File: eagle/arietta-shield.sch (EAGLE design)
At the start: 11 parts

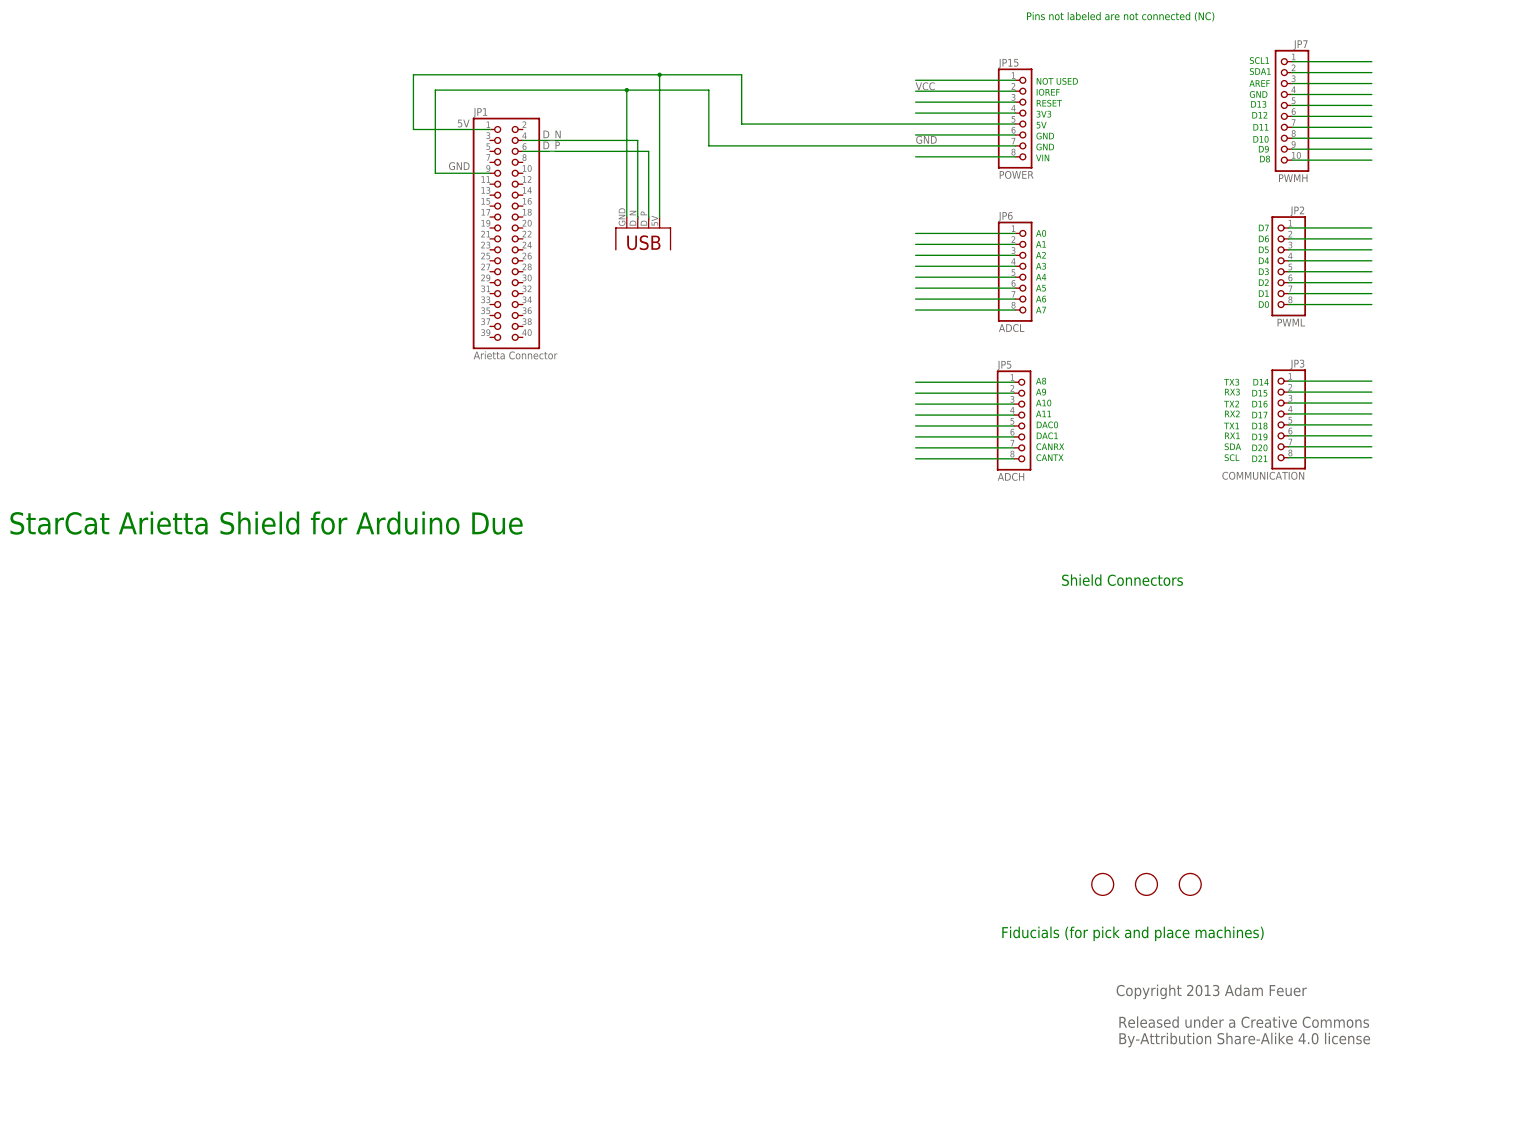
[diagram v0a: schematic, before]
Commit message: added unpopulated SPI and rear connectors
- 5V now only connected to USB now, not shield connector,
  enabling connection to another computer when connected to
  the Arduino Due
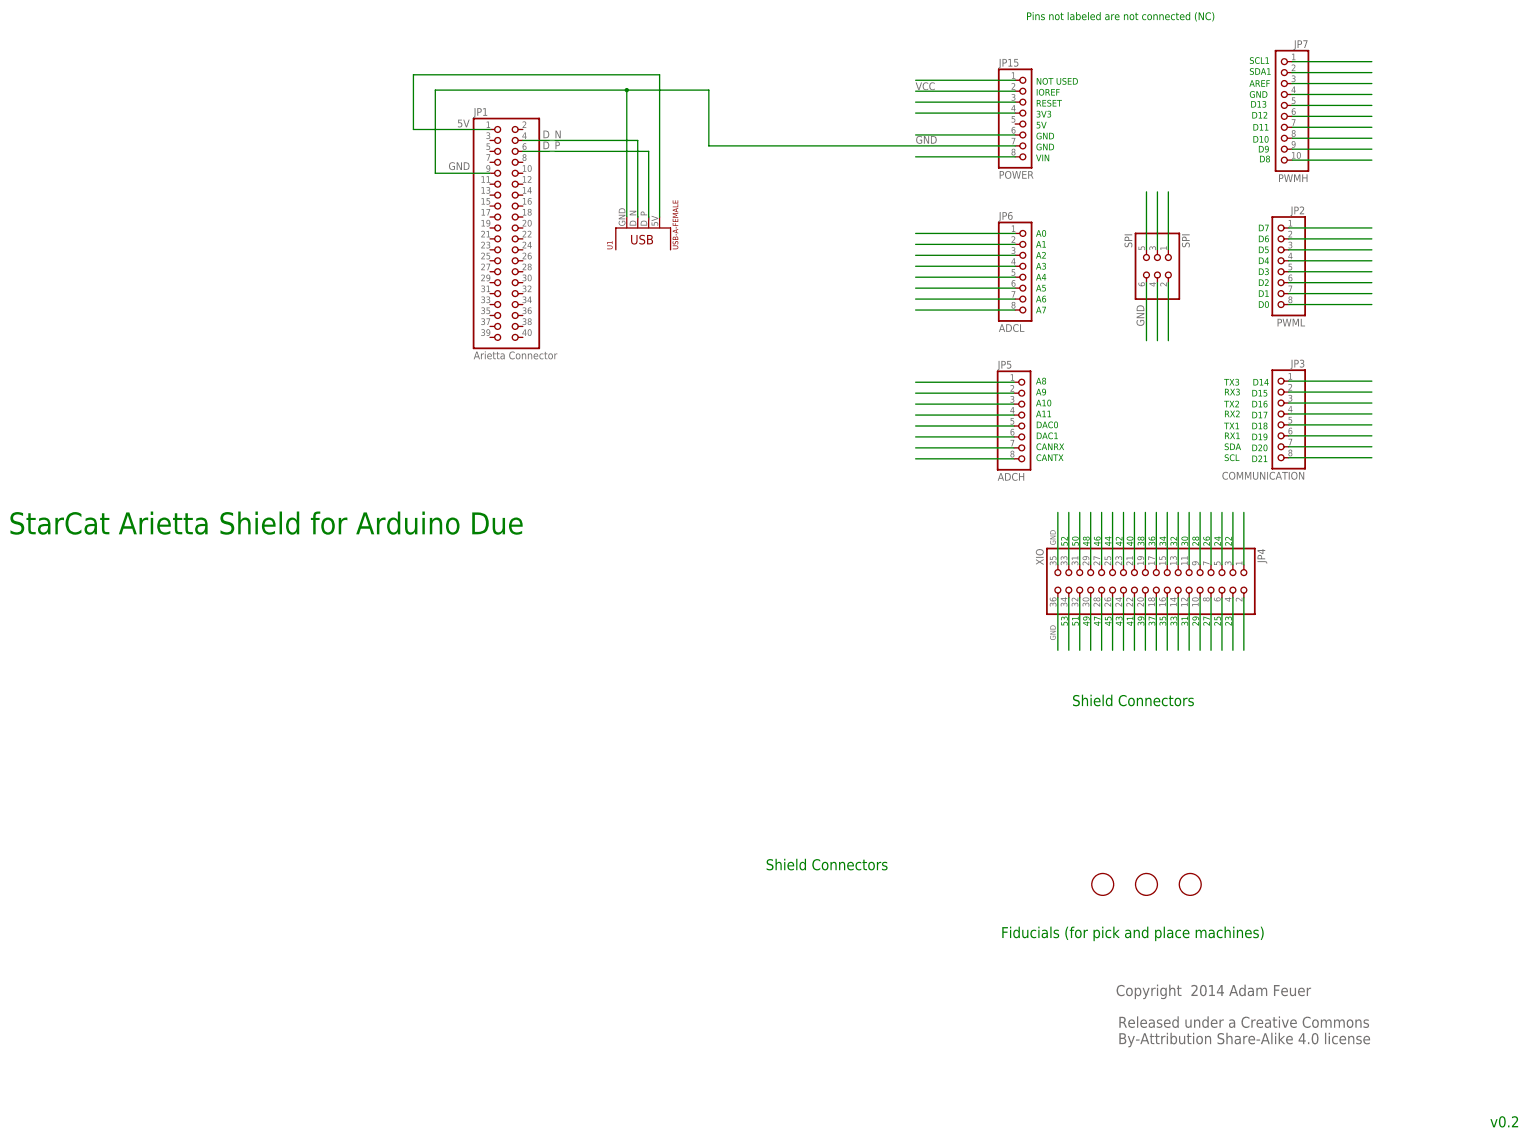
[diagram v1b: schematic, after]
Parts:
- added JP4: XIO, SmartPrj:PINHD-2X18
- added SPI: SPI, SmartPrj:PINHD-2X3
- renumbered U$7 to U1
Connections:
- new net D38: JP4.19
- new net D39: JP4.20
- new net D40: JP4.21
- new net D41: JP4.22
- new net D42: JP4.23
- new net D43: JP4.24
- new net D44: JP4.25
- new net D45: JP4.26
- new net N$109: JP4.31
- new net N$115: JP4.1
- new net N$116: JP4.2
- new net N$580: JP4.5
- new net N$581: JP4.7
- new net N$582: JP4.11
- new net N$583: JP4.13
- new net N$584: JP4.27
- new net N$585: JP4.29
- new net N$586: JP4.33
- new net N$587: JP4.4
- new net N$588: JP4.6
- new net N$589: JP4.8
- new net N$590: JP4.12
- new net N$591: JP4.14
- new net N$592: JP4.30
- new net N$601: JP4.28
- new net N$73: JP4.34
- new net N$74: JP4.32
- new net N$89: JP4.18
- new net N$91: JP4.16
- new net N$92: JP4.10
- new net N$93: JP4.3
- new net N$94: JP4.9
- new net N$96: JP4.15
- new net N$97: JP4.17
- new net RESET: SPI.5
- new net SPI0_MISO: SPI.1
- new net SPI0_MOSI: SPI.4
- new net SPI0_SCK: SPI.3
- new net VCC_5V: SPI.2
- net 5V: no longer JP15.5
- net GND: now also JP4.35, JP4.36, SPI.6
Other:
- note added: "22"
- note added: "23"
- note added: "24"
- note added: "25"
- note added: "26"
- note added: "27"
- note added: "28"
- note added: "29"
- note added: "30"
- note added: "31"
- note added: "32"
- note added: "33"
- note added: "34"
- note added: "35"
- note added: "36"
- note added: "37"
- note added: "38"
- note added: "39"
- note added: "40"
- note added: "41"
- note added: "42"
- note added: "43"
- note added: "44"
- note added: "45"
- note added: "46"
- note added: "47"
- note added: "48"
- note added: "49"
- note added: "50"
- note added: "51"
- note added: "52"
- note added: "53"
- note added: "Copyright 2014 Adam Feuer"
- note added: "v0.2"
- note removed: "Copyright 2013 Adam Feuer"
